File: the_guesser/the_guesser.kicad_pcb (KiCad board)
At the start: 4 copper layers, 24 x 72 mm, 73 parts, among them J3 BMI-S-209-F, J4 Screw_Terminal_01x06, J5 Screw_Terminal_01x06, J6 BMI-S-209-F, J7 USB_C_Receptacle_USB2.0_16P, U1 ESP32-S3, U10 TPS61033DRLR, U11 W25Q128JVS, U12 MMC5883MA, U2 CC1101RGPR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

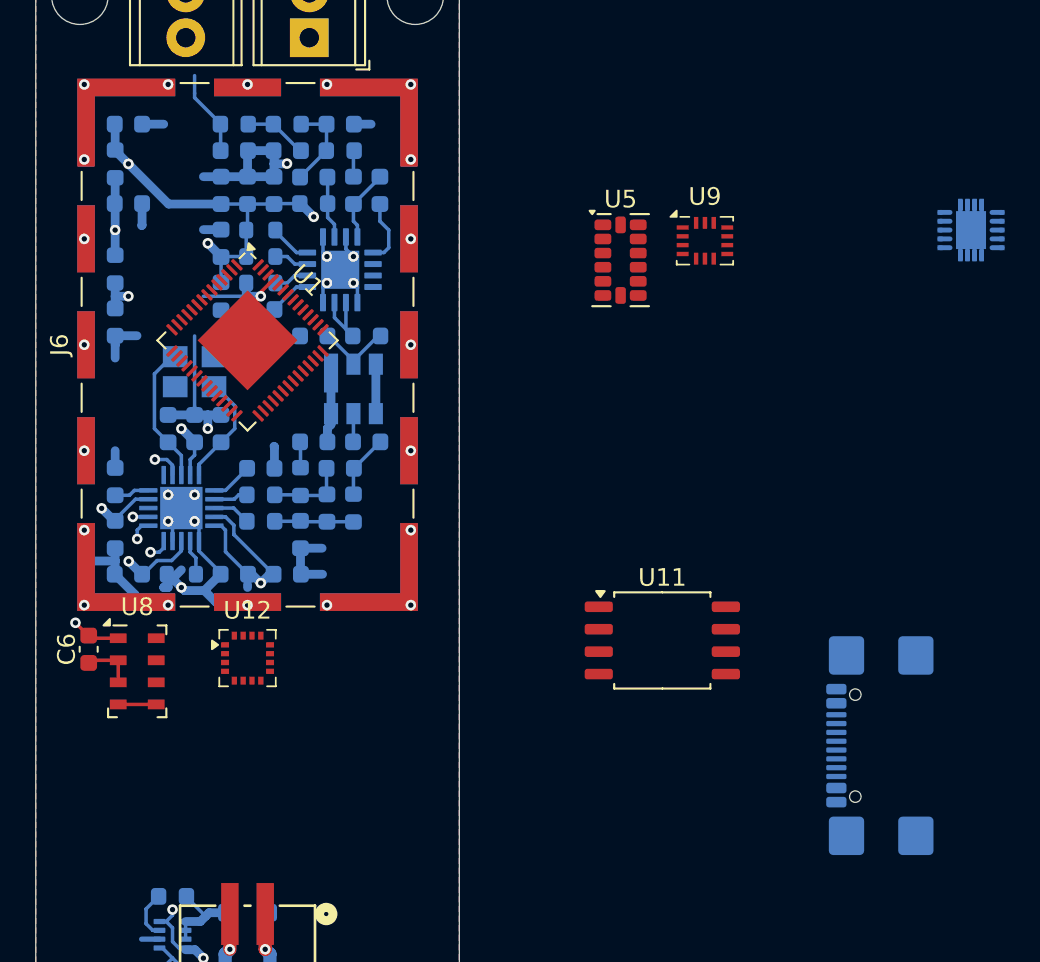
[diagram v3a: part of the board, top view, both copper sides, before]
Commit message: Finished Guesser sensor selection and started sensor routing
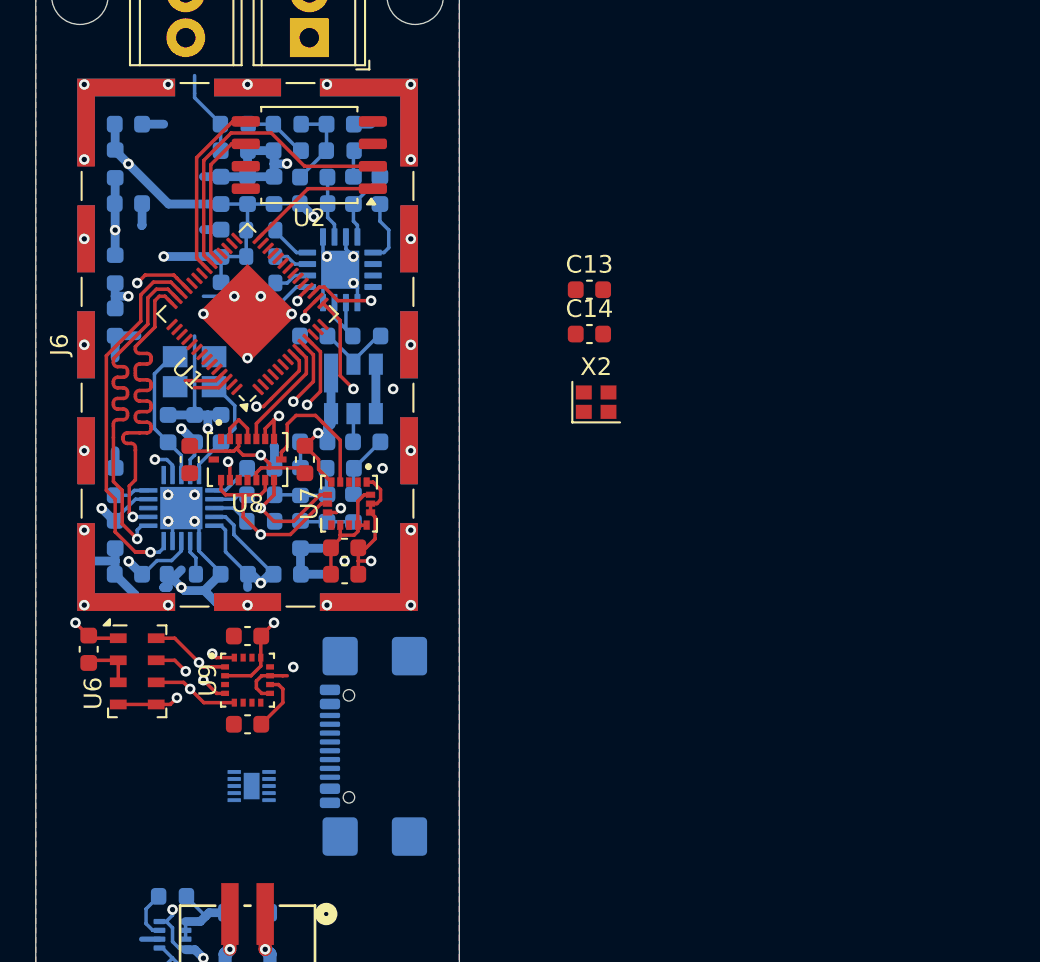
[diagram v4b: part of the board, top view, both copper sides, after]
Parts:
- removed the U5 at (233.1, 55.5)
- added C10: 10u, Capacitor_SMD:C_0603_1608Metric, F.Cu at (212.0, 81.8)
- added C11: 100n, Capacitor_SMD:C_0603_1608Metric, F.Cu at (208.7, 66.8)
- added C12: 100n, Capacitor_SMD:C_0603_1608Metric, F.Cu at (215.2, 66.8)
- added C13: ???, Capacitor_SMD:C_0603_1608Metric, F.Cu at (231.4, 57.1)
- added C14: ???, Capacitor_SMD:C_0603_1608Metric, F.Cu at (231.4, 59.6)
- added C7: 0.1u, Capacitor_SMD:C_0603_1608Metric, F.Cu at (217.5, 71.8)
- added C8: 10u, Capacitor_SMD:C_0603_1608Metric, F.Cu at (217.5, 73.2)
- added C9: 1u, Capacitor_SMD:C_0603_1608Metric, F.Cu at (212.0, 76.8)
- added U13: TPD4S014DSQR, locals_but_working_PLEASE:TPD4S014DSQR, B.Cu at (212.2, 85.2)
- added X2: XRCGB40M000F1S2GR0, Crystal:Crystal_SMD_2016-4Pin_2.0x1.6mm, F.Cu at (231.8, 63.5)
- U1: value ESP32-S3 -> ESP32-S3FN8
- U3: renamed from U2; footprint locals_but_working_PLEASE:QFN50P400X400X100-21N -> locals_but_working_PLEASE:CC1101RGPR
- U4: renamed from U3; footprint locals_but_working_PLEASE:QFN65P400X400X100-17N -> locals_but_working_PLEASE:CC1190RGVR
- U7: value TPD4S014 -> H3LIS200DLTR; footprint Package_SON:Texas_S-PWSON-N10 -> locals_but_working_PLEASE:H3LIS200DLTR; moved to F.Cu
- U8: renamed from U9; value BMI160 -> BMI088; footprint Package_LGA:Bosch_LGA-14_3x2.5mm_P0.5mm -> locals_but_working_PLEASE:BMI088
- U9: renamed from U12; footprint Package_LGA:LGA-16_3x3mm_P0.5mm -> locals_but_working_PLEASE:MMC5983MA
- moved U7 38.5 mm to (217.8, 69.2), turned to -90 degrees
- moved U2 34.0 mm to (215.5, 49.5), turned to 180 degrees
- moved U8 28.7 mm to (212.0, 66.8)
- moved J7 28.7 mm to (220.3, 83.0)
- moved U1 1.50 mm to (212.0, 58.5), turned to 135 degrees
- moved U9 1.25 mm to (212.0, 79.2)
- renumbered U11 to U2, U4 to U5, U8 to U6
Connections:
- U1 pad 10: unconnected-(U1-GPIO5-Pad10) -> ~{CS}_{HIGH_ACC}
- U1 pad 11: unconnected-(U1-GPIO6-Pad11) -> ~{CS}_{MAG}
- U1 pad 14: SCLK2 -> unconnected-(U1-GPIO9-Pad14)
- U1 pad 15: SDI2 -> ~{CS}_{BARO}
- U1 pad 16: SDO2 -> SDI2
- U1 pad 17: unconnected-(U1-GPIO12-Pad17) -> SCLK2
- U1 pad 18: unconnected-(U1-GPIO13-Pad18) -> SDO2
- U1 pad 28: unconnected-(U1-SPICS1-Pad28) -> ~{CS}_{FLASH}
- U1 pad 33: unconnected-(U1-SPICLK-Pad33) -> SCLK1
- U1 pad 34: unconnected-(U1-SPIQ-Pad34) -> SDO1
- U1 pad 35: unconnected-(U1-SPID-Pad35) -> SDI1
- U1 pad 39: unconnected-(U1-GPIO34-Pad39) -> ~{CS}_{RF}
- U1 pad 40: unconnected-(U1-GPIO35-Pad40) -> SDI3
- U1 pad 41: unconnected-(U1-GPIO36-Pad41) -> SCLK3
- U1 pad 42: unconnected-(U1-GPIO37-Pad42) -> SDO3
- U1 pad 53: unconnected-(U1-XTAL_N-Pad53) -> XTAL_N
- U1 pad 54: unconnected-(U1-XTAL_P-Pad54) -> XTAL_P
- U1 pad 8: unconnected-(U1-GPIO3-Pad8) -> ~{CS}_{MAIN_ACC}
- U1 pad 9: unconnected-(U1-GPIO4-Pad9) -> ~{CS}_{GYRO}
- U2 pad 2: SDO2 -> SDO1
- U2 pad 5: SDI2 -> SDI1
- U2 pad 6: SCLK2 -> SCLK1
- U3 pad 1: SCLK2 -> SCLK3
- U3 pad 2: SDO2 -> SDO3
- U3 pad 20: SDI2 -> SDI3
- U6 pad 6: SDO1 -> SDO2
- U6 pad 7: SDI1 -> SDI2
- U6 pad 8: SCLK1 -> SCLK2
- U7 pad 1: Net-(U7-VBUSOUT-Pad1) -> VCC
- U7 pad 10: Net-(U7-VBUS-Pad10) -> GND
- U7 pad 2: Net-(U7-VBUSOUT-Pad1) -> unconnected-(U7-NC-Pad2)
- U7 pad 4: unconnected-(U7-~{ACK}-Pad4) -> SCLK2
- U7 pad 5: unconnected-(U7-ID-Pad5) -> GND
- U7 pad 6: USB_D- -> SDI2
- U7 pad 7: USB_D+ -> SDO2
- U7 pad 8: GND -> ~{CS}_{HI_ACC}
- U7 pad 9: Net-(U7-VBUS-Pad10) -> unconnected-(U7-INT_2-Pad9)
- U8 pad 10: unconnected-(U9-OCSB-Pad10) -> SDO2
- U8 pad 11: unconnected-(U9-OSDO-Pad11) -> VCC
- U8 pad 14: unconnected-(U9-SDx-Pad14) -> ~{CS}_{MAIN_ACC}
- U8 pad 2: unconnected-(U9-ASDx-Pad2) -> GND
- U8 pad 3: unconnected-(U9-ASCx-Pad3) -> VCC
- U8 pad 4: unconnected-(U9-INT1-Pad4) -> GND
- U8 pad 5: unconnected-(U9-VDDIO-Pad5) -> ~{CS}_{GYRO}
- U8 pad 6: unconnected-(U9-GNDIO-Pad6) -> GND
- U8 pad 8: unconnected-(U9-VDD-Pad8) -> SCLK2
- U8 pad 9: unconnected-(U9-INT2-Pad9) -> SDI2
- U9 pad 1: SCL -> SCLK2
- U9 pad 10: unconnected-(U12-CAP-Pad10) -> Net-(U9-CAP)
- U9 pad 13: unconnected-(U12-VDDIO-Pad13) -> VCC
- U9 pad 16: SDA -> SDI2
- U9 pad 2: unconnected-(U12-VDD-Pad2) -> VCC
- U9 pad 4: unconnected-(U12-NC-Pad4) -> ~{CS}_{MAG}
- U9 pad 5: unconnected-(U12-NC-Pad5) -> SDO2
- X1 pad 2: unconnected-(X1-Pad2) -> GND
- X1 pad 4: unconnected-(X1-Pad4) -> GND
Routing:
- net SDO2: track 0.88 -> 61.1 mm, vias 1 -> 4
- net SDI2: track 0.85 -> 51.6 mm, vias 1 -> 5
- net SCLK2: track 0.85 -> 47.6 mm, vias 1 -> 4
- net VCC: track 15.9 -> 37.9 mm, vias 4 -> 7
- net SDO3: track 0.00 -> 21.6 mm, vias 0 -> 1
- net SDI3: track 0.00 -> 21.4 mm, vias 0 -> 1
- net SCLK3: track 0.00 -> 21.4 mm, vias 0 -> 1
- net SDO1: track 0.00 -> 17.0 mm
- net GND: track 71.4 -> 87.5 mm, vias 32 -> 37
- net ~{CS}_{RF}: track 1.69 -> 16.7 mm, vias 1 -> 2
- net SDI1: track 0.00 -> 10.2 mm
- net ~{CS}_{MAIN_ACC}: track 0.00 -> 9.21 mm, vias 0 -> 2
- net SCLK1: track 0.00 -> 7.92 mm
- net ~{CS}_{FLASH}: track 0.00 -> 7.67 mm
- net ~{CS}_{BARO}: track 2.15 -> 9.04 mm, vias 0 -> 2
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
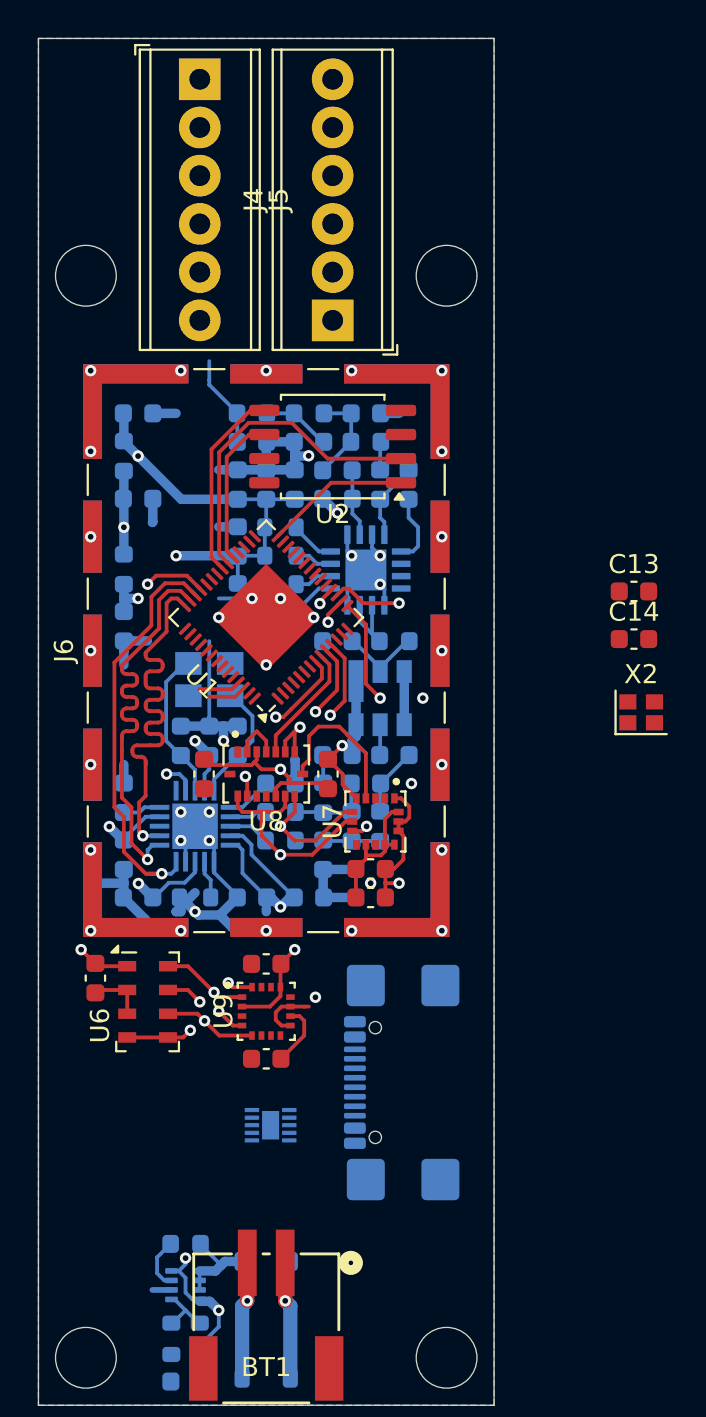
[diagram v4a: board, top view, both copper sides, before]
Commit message: Routed USB and SPI buses
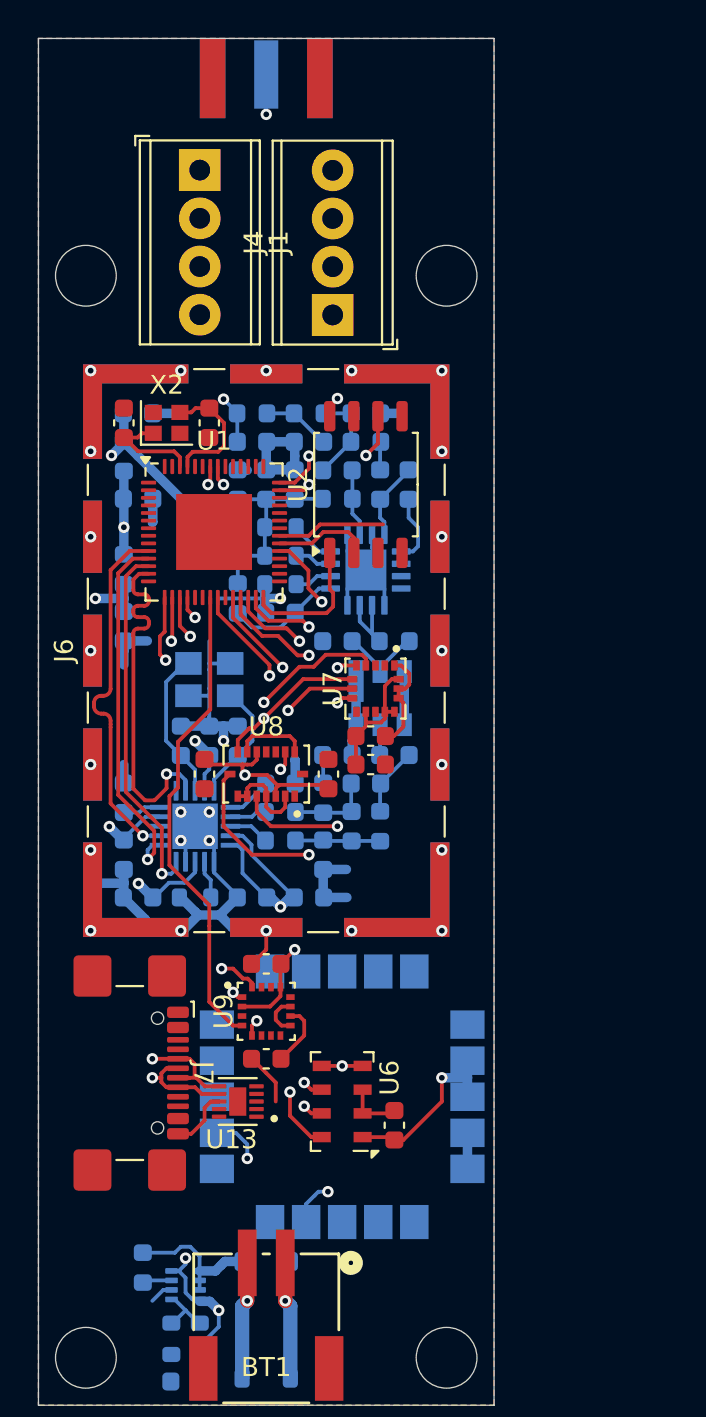
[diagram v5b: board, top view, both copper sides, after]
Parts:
- removed J5: Screw_Terminal_01x06, TerminalBlock_Phoenix:TerminalBlock_Phoenix_MPT-0,5-6-2.54_1x06_P2.54mm_Horizontal
- added J1: Screw_Terminal_01x06, TerminalBlock_Phoenix:TerminalBlock_Phoenix_MPT-0,5-4-2.54_1x04_P2.54mm_Horizontal, F.Cu at (208.5, 34.9)
- added J2: Conn_Coaxial, Connector_Coaxial:SMA_Samtec_SMA-J-P-X-ST-EM1_EdgeMount, B.Cu at (212.0, 30.1)
- added U11: SAM-M8Q, RF_GPS:ublox_SAM-M8Q, B.Cu at (216.0, 83.8)
- J4: footprint TerminalBlock_Phoenix:TerminalBlock_Phoenix_MPT-0,5-6-2.54_1x06_P2.54mm_Horizontal -> TerminalBlock_Phoenix:TerminalBlock_Phoenix_MPT-0,5-4-2.54_1x04_P2.54mm_Horizontal
- J7, U13: moved to F.Cu
- moved X2 29.3 mm to (206.8, 48.2)
- moved C13 28.3 mm to (204.5, 48.2), turned to 90 degrees
- moved C14 25.1 mm to (209.0, 48.2), turned to 90 degrees
- moved C6 17.6 mm to (218.8, 85.2), turned to 90 degrees
- moved J7 16.7 mm to (203.7, 82.5)
- moved U6 11.5 mm to (216.0, 84.0), turned to 180 degrees
- moved C7 7.00 mm to (217.5, 64.8)
- moved C8 7.00 mm to (217.5, 66.2)
- moved U7 7.00 mm to (217.8, 62.2)
- moved C11 6.55 mm to (215.3, 66.8), turned to 90 degrees
- moved C12 6.50 mm to (208.8, 66.8), turned to -90 degrees
- moved U1 5.27 mm to (209.2, 54.0), turned to 0 degrees
- moved U2 2.66 mm to (217.2, 51.5), turned to 90 degrees
- moved L3 2.57 mm to (205.5, 92.8), turned to 90 degrees
- moved U13 2.13 mm to (210.5, 84.0), turned to 180 degrees
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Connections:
- U1 pad 10: ~{CS}_{HIGH_ACC} -> SDO3
- U1 pad 11: ~{CS}_{MAG} -> SCLK3
- U1 pad 12: unconnected-(U1-GPIO7-Pad12) -> SDI3
- U1 pad 13: unconnected-(U1-GPIO8-Pad13) -> ~{CS}_{RF}
- U1 pad 15: ~{CS}_{BARO} -> ~{CS}_{MAIN_ACC}
- U1 pad 21: unconnected-(U1-XTAL_32K_P-Pad21) -> ~{CS}_{MAG}
- U1 pad 22: unconnected-(U1-XTAL_32K_N-Pad22) -> ~{CS}_{GYRO}
- U1 pad 24: unconnected-(U1-GPIO18-Pad24) -> ~{CS}_{BARO}
- U1 pad 27: unconnected-(U1-GPIO21-Pad27) -> ~{CS}_{HI_ACC}
- U1 pad 39: ~{CS}_{RF} -> unconnected-(U1-GPIO34-Pad39)
- U1 pad 40: SDI3 -> unconnected-(U1-GPIO35-Pad40)
- U1 pad 41: SCLK3 -> SCL1
- U1 pad 42: SDO3 -> SDA1
- U1 pad 8: ~{CS}_{MAIN_ACC} -> unconnected-(U1-GPIO3-Pad8)
- U1 pad 9: ~{CS}_{GYRO} -> unconnected-(U1-GPIO4-Pad9)
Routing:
- net USB_D-: track 0.00 -> 58.6 mm, vias 0 -> 2
- net SCL1: track 0.00 -> 58.0 mm, vias 0 -> 2
- net USB_D+: track 0.00 -> 57.8 mm, vias 0 -> 2
- net SDA1: track 0.00 -> 54.9 mm, vias 0 -> 2
- net ~{CS}_{BARO}: track 9.04 -> 30.1 mm
- net SDO2: track 61.1 -> 40.5 mm
- net ~{CS}_{MAG}: track 5.84 -> 25.3 mm, vias 2 -> 0
- net Net-(J2-In): track 4.84 -> 20.5 mm, vias 0 -> 2
- net ~{CS}_{GYRO}: track 6.44 -> 20.1 mm, vias 0 -> 2
- net SDO1: track 17.0 -> 5.09 mm
- net ~{CS}_{HI_ACC}: track 0.86 -> 10.5 mm, vias 1 -> 2
- net VCC_{CC1190}: track 37.8 -> 28.2 mm, vias 3 -> 1
- net SCLK1: track 7.92 -> 14.9 mm, vias 0 -> 2
- net SDI2: track 51.6 -> 45.9 mm, vias 5 -> 4
- net VCC: track 37.9 -> 43.3 mm
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
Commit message: Routed Guesser pyro channels
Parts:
- added Q1: AS2312, Package_TO_SOT_SMD:SOT-23, B.Cu at (204.5, 28.0)
- added Q2: AS2312, Package_TO_SOT_SMD:SOT-23, B.Cu at (204.5, 31.5)
- added Q3: AS2312, Package_TO_SOT_SMD:SOT-23, B.Cu at (204.5, 35.0)
- added Q4: AS2312, Package_TO_SOT_SMD:SOT-23, B.Cu at (219.5, 35.0)
- added Q5: AS2312, Package_TO_SOT_SMD:SOT-23, B.Cu at (219.5, 31.5)
- added Q6: AS2312, Package_TO_SOT_SMD:SOT-23, B.Cu at (219.5, 28.0)
- added R4: 10k, Resistor_SMD:R_0603_1608Metric, B.Cu at (201.8, 28.0)
- added R5: 10k, Resistor_SMD:R_0603_1608Metric, B.Cu at (201.8, 31.5)
- added R6: 10k, Resistor_SMD:R_0603_1608Metric, B.Cu at (201.8, 35.0)
- added R7: 10k, Resistor_SMD:R_0603_1608Metric, B.Cu at (222.2, 35.0)
- added R8: 10k, Resistor_SMD:R_0603_1608Metric, B.Cu at (222.2, 31.5)
- added R9: 10k, Resistor_SMD:R_0603_1608Metric, B.Cu at (222.2, 28.0)
- moved J2 3.00 mm to (212.0, 27.1)
- moved J1 2.76 mm to (208.2, 32.2)
- moved J4 2.76 mm to (215.8, 39.8)
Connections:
- J1 pad 1: unconnected-(J1-Pin_1-Pad1) -> C_{1}
- J1 pad 2: unconnected-(J1-Pin_2-Pad2) -> C_{2}
- J1 pad 3: unconnected-(J1-Pin_3-Pad3) -> C_{3}
- J1 pad 4: unconnected-(J1-Pin_4-Pad4) -> GND
- J4 pad 1: unconnected-(J4-Pin_1-Pad1) -> GND
- J4 pad 2: unconnected-(J4-Pin_2-Pad2) -> C_{4}
- J4 pad 3: unconnected-(J4-Pin_3-Pad3) -> C_{5}
- J4 pad 4: unconnected-(J4-Pin_4-Pad4) -> C_{6}
- U1 pad 43: unconnected-(U1-GPIO38-Pad43) -> T_{4}
- U1 pad 44: unconnected-(U1-MTCK-Pad44) -> T_{5}
- U1 pad 45: unconnected-(U1-MTDO-Pad45) -> T_{6}
- U1 pad 47: unconnected-(U1-MTDI-Pad47) -> T_{1}
- U1 pad 48: unconnected-(U1-MTMS-Pad48) -> T_{2}
- U1 pad 49: unconnected-(U1-U0TXD-Pad49) -> T_{3}
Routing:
- net GND: track 89.9 -> 134.8 mm, vias 27 -> 33
- net T_{6}: track 0.00 -> 29.7 mm, vias 0 -> 2
- net T_{1}: track 0.00 -> 28.7 mm, vias 0 -> 2
- net T_{2}: track 0.00 -> 28.5 mm, vias 0 -> 2
- net T_{5}: track 0.00 -> 26.0 mm, vias 0 -> 2
- net T_{3}: track 0.00 -> 23.3 mm, vias 0 -> 2
- net T_{4}: track 0.00 -> 22.4 mm, vias 0 -> 2
- net VCC_{CC1190}: track 28.2 -> 38.1 mm, vias 1 -> 2
- net SDI1: track 5.70 -> 11.8 mm
- net VCC: track 43.3 -> 49.1 mm, vias 7 -> 8
- net C_{6}: track 0.00 -> 5.67 mm
- net C_{1}: track 0.00 -> 5.66 mm
- net C_{5}: track 0.00 -> 5.27 mm
- net C_{2}: track 0.00 -> 5.27 mm
- net VCC_{CC1101}: track 54.4 -> 59.5 mm
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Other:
- board size 24 x 72 mm -> 24 x 75 mm
